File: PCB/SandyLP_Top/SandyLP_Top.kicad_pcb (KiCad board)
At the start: 2 copper layers, 74.9 x 37 mm, 31 parts

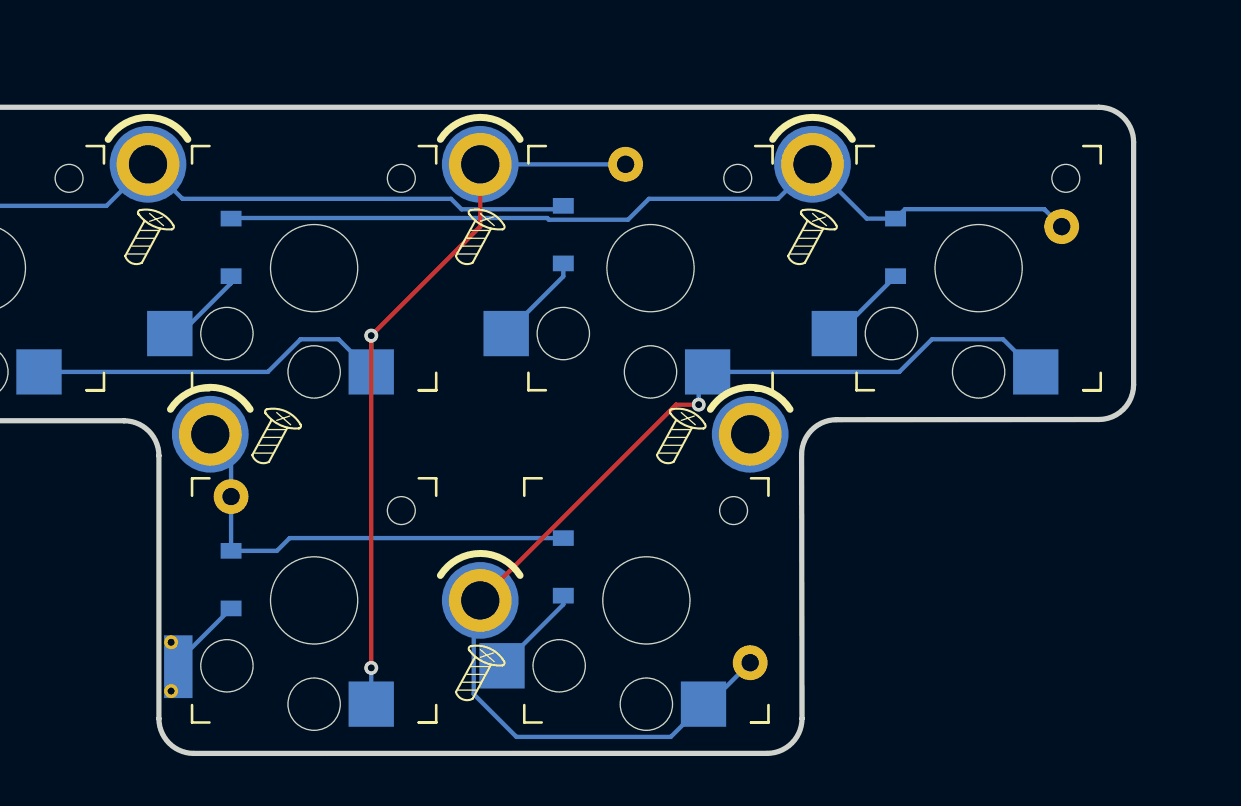
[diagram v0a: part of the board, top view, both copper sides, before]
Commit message: スイッチの位置ずれ修正。ネジ位置調整。
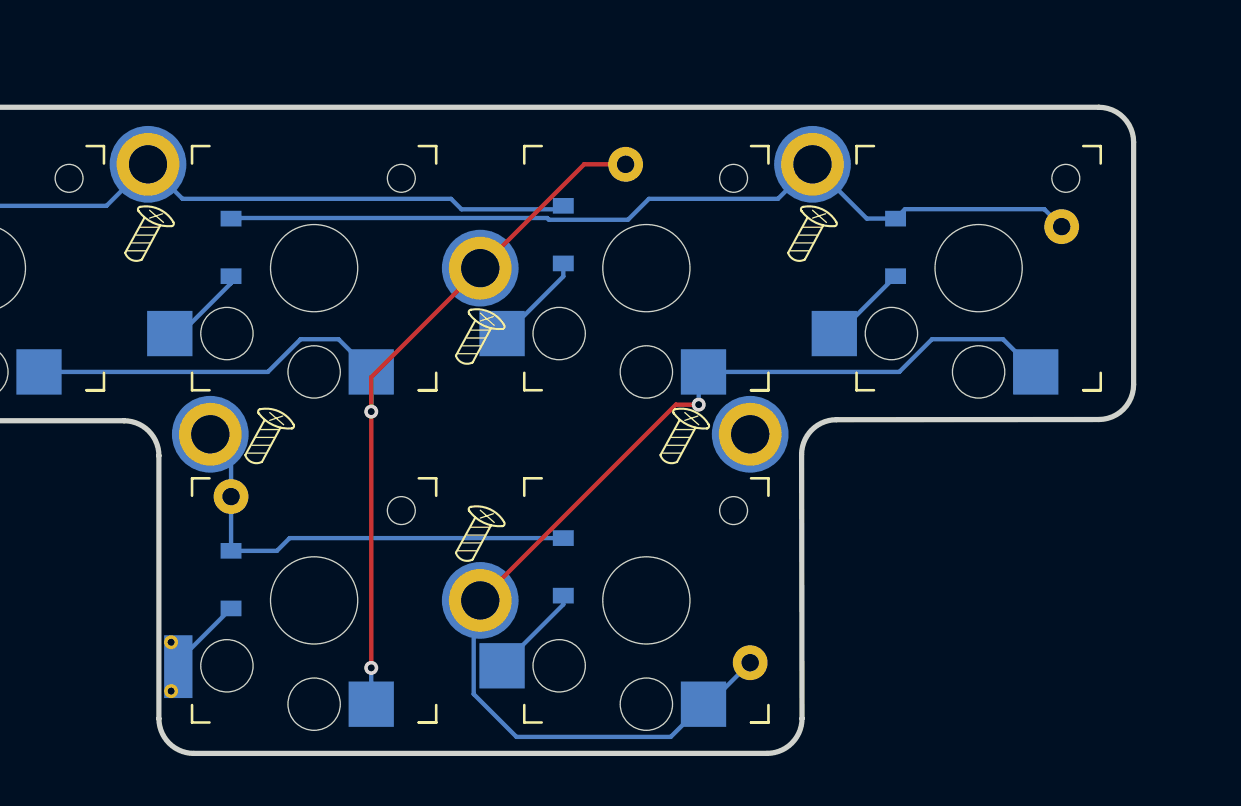
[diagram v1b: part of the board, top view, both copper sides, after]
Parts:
- moved REF** 7.99 mm to (157.9, 63.9)
- moved H2 5.95 mm to (158.0, 46.1)
- moved REF** 5.72 mm to (157.9, 52.6)
- moved REF** 0.40 mm to (145.8, 58.3)
- moved SW_Y1 0.24 mm to (167.5, 46.1)
- moved REF** 0.20 mm to (169.6, 58.3)
- moved REF** 0.18 mm to (138.9, 46.7)
- moved REF** 0.18 mm to (176.9, 46.7)
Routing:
- net Top_col3: track 64.6 -> 61.3 mm

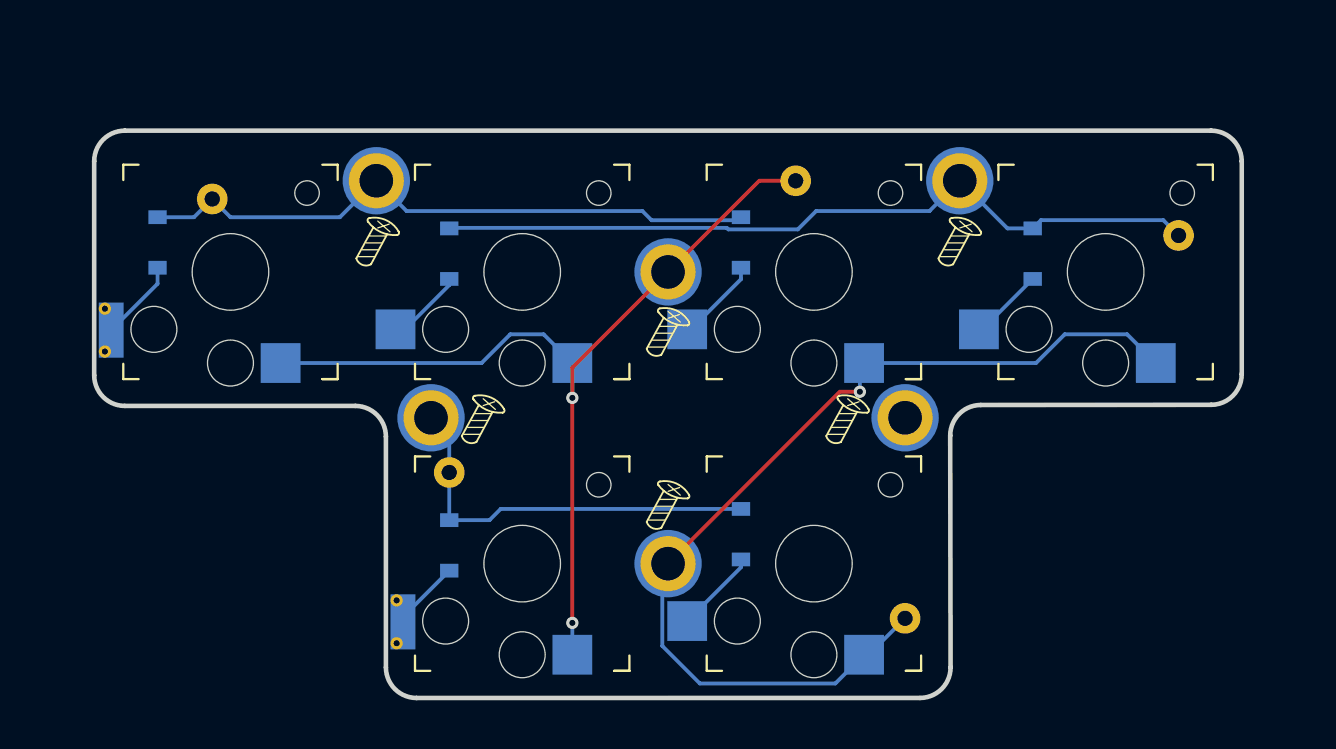
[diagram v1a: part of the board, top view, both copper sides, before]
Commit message: 配線完了。ビア打ちまだ。
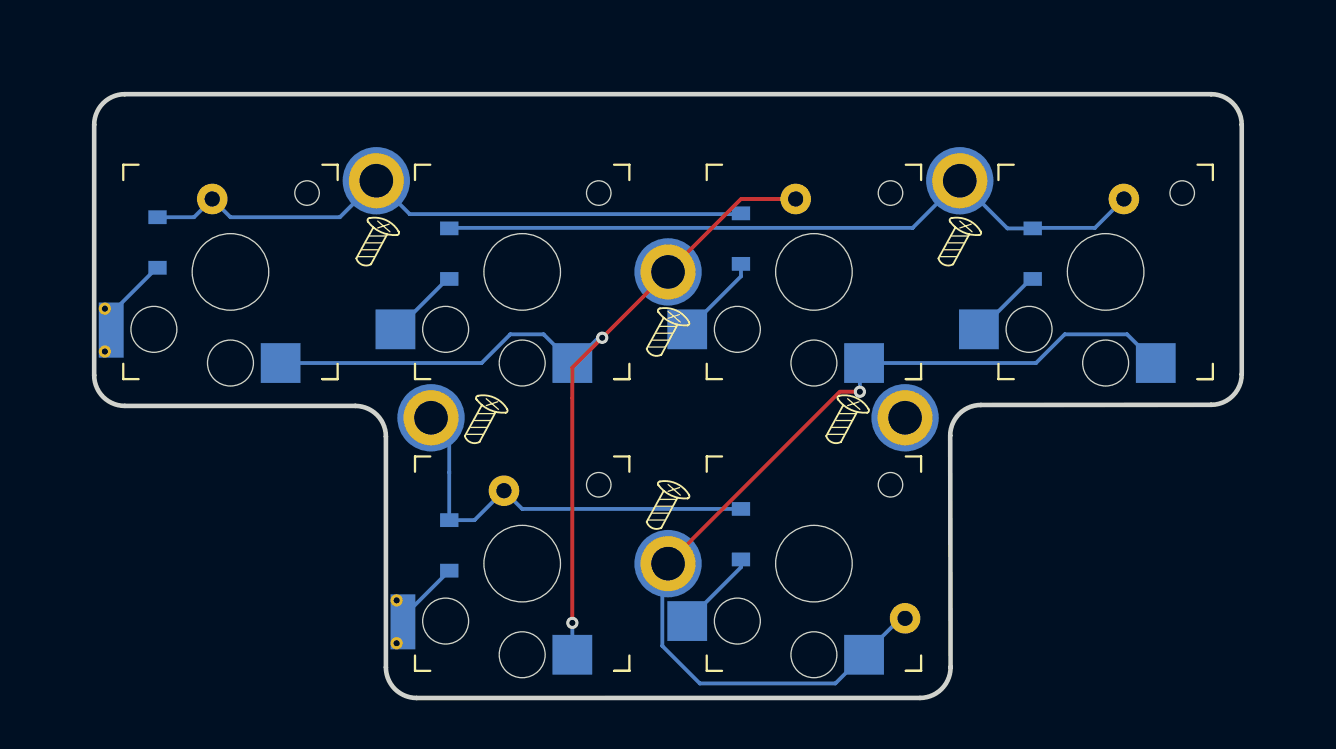
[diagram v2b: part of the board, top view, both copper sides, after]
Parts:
- removed ?: , clipboard:1d23b097-72e0-487b-bec7-a328ee8b6ed7
- moved EXT_TR4 4.29 mm to (187.7, 41.3)
- moved EXT_TR1 3.77 mm to (147.3, 60.3)
- moved EXT_TC3 1.19 mm to (166.3, 41.3)
- moved D3 0.25 mm to (162.7, 43.9)
- moved REF** 0.20 mm to (146.0, 58.3)
- turned EXT_TR0 to 180 degrees
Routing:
- net Top_row4: track 50.9 -> 47.4 mm
- net Top_row1: track 26.5 -> 27.5 mm
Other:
- board size 74.9 x 37 mm -> 74.9 x 39.4 mm

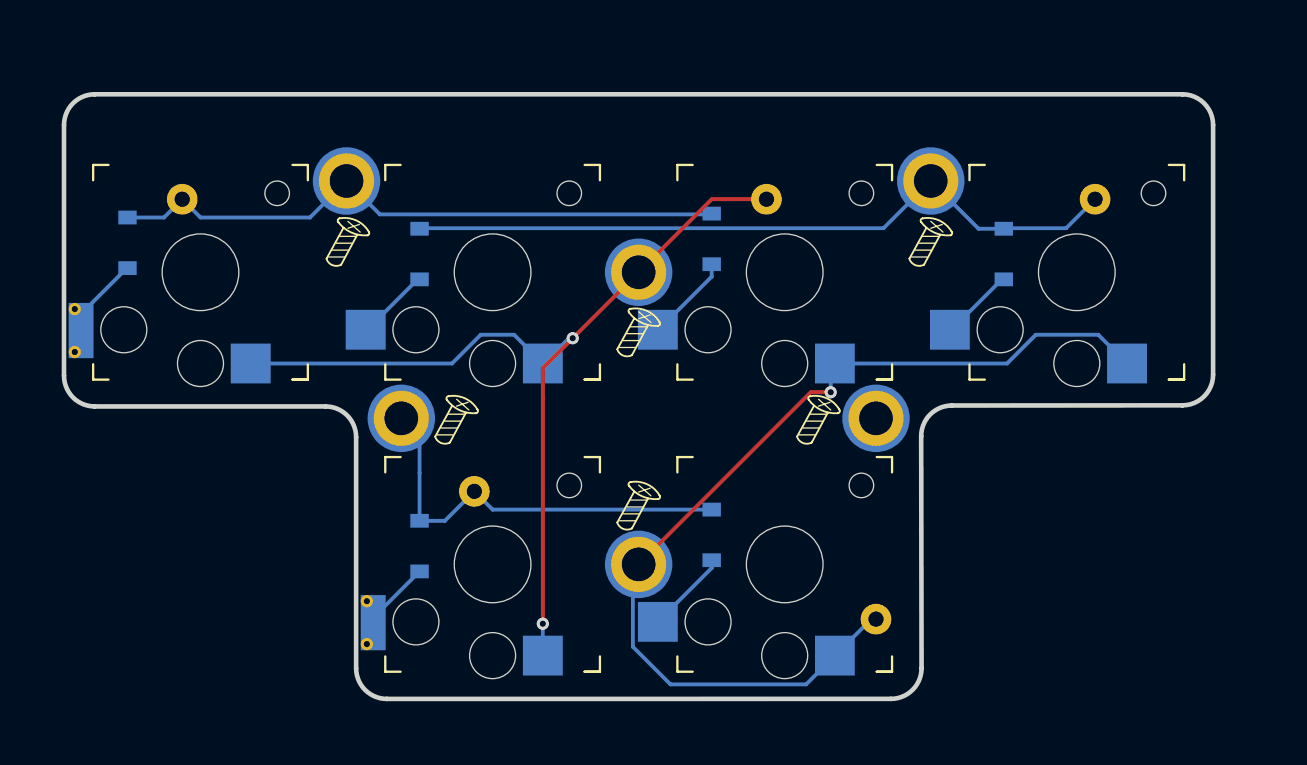
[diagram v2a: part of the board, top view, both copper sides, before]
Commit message: 後からねじ止めするアイコン（＝ドライバー）に変更
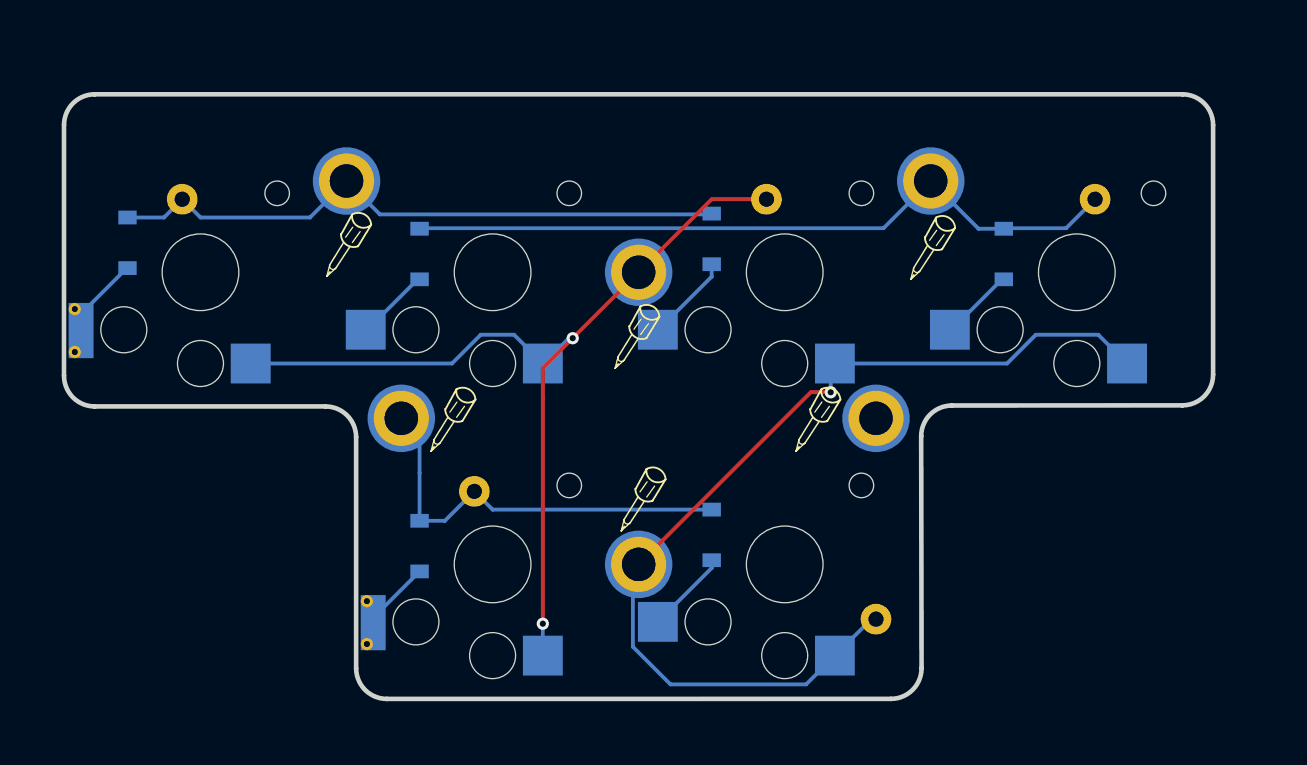
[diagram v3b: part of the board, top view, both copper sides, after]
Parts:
- REF** (x6): value ICON_Screw_Medium -> ICON_ScrewDriver_Medium; footprint locallib:ICON_Screw_Medium -> locallib:ICON_ScrewDriver_Medium
- moved REF** 0.93 mm to (176.9, 47.6)
- moved REF** 0.86 mm to (157.7, 53.4)
- moved REF** 0.73 mm to (138.9, 47.4)
- moved REF** 0.64 mm to (145.7, 58.8)
- moved REF** 0.55 mm to (169.5, 58.8)
- moved REF** 0.21 mm to (158.1, 64.0)

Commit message: ネジ穴のアイコンを更新
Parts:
- added REF**: ICON_arrow_round_small, locallib:ICON_arrow_round_small, F.Cu at (156.9, 71.2)
- added REF**: ICON_arrow_round_small, locallib:ICON_arrow_round_small, F.Cu at (156.7, 53.1)
- added REF**: ICON_arrow_round_small, locallib:ICON_arrow_round_small, F.Cu at (175.9, 47.1)
- added REF**: ICON_arrow_round_small, locallib:ICON_arrow_round_small, F.Cu at (168.5, 58.5)
- added REF**: ICON_arrow_round_small, locallib:ICON_arrow_round_small, F.Cu at (137.9, 47.1)
- added REF**: ICON_arrow_round_small, locallib:ICON_arrow_round_small, F.Cu at (144.7, 58.5)
- REF** (x6): value ICON_ScrewDriver_Medium -> ICON_Screw_Medium; footprint locallib:ICON_ScrewDriver_Medium -> locallib:ICON_Screw_Medium
- moved REF** 7.67 mm to (157.8, 71.7)
